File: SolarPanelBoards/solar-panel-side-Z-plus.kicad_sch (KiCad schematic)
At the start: 39 parts

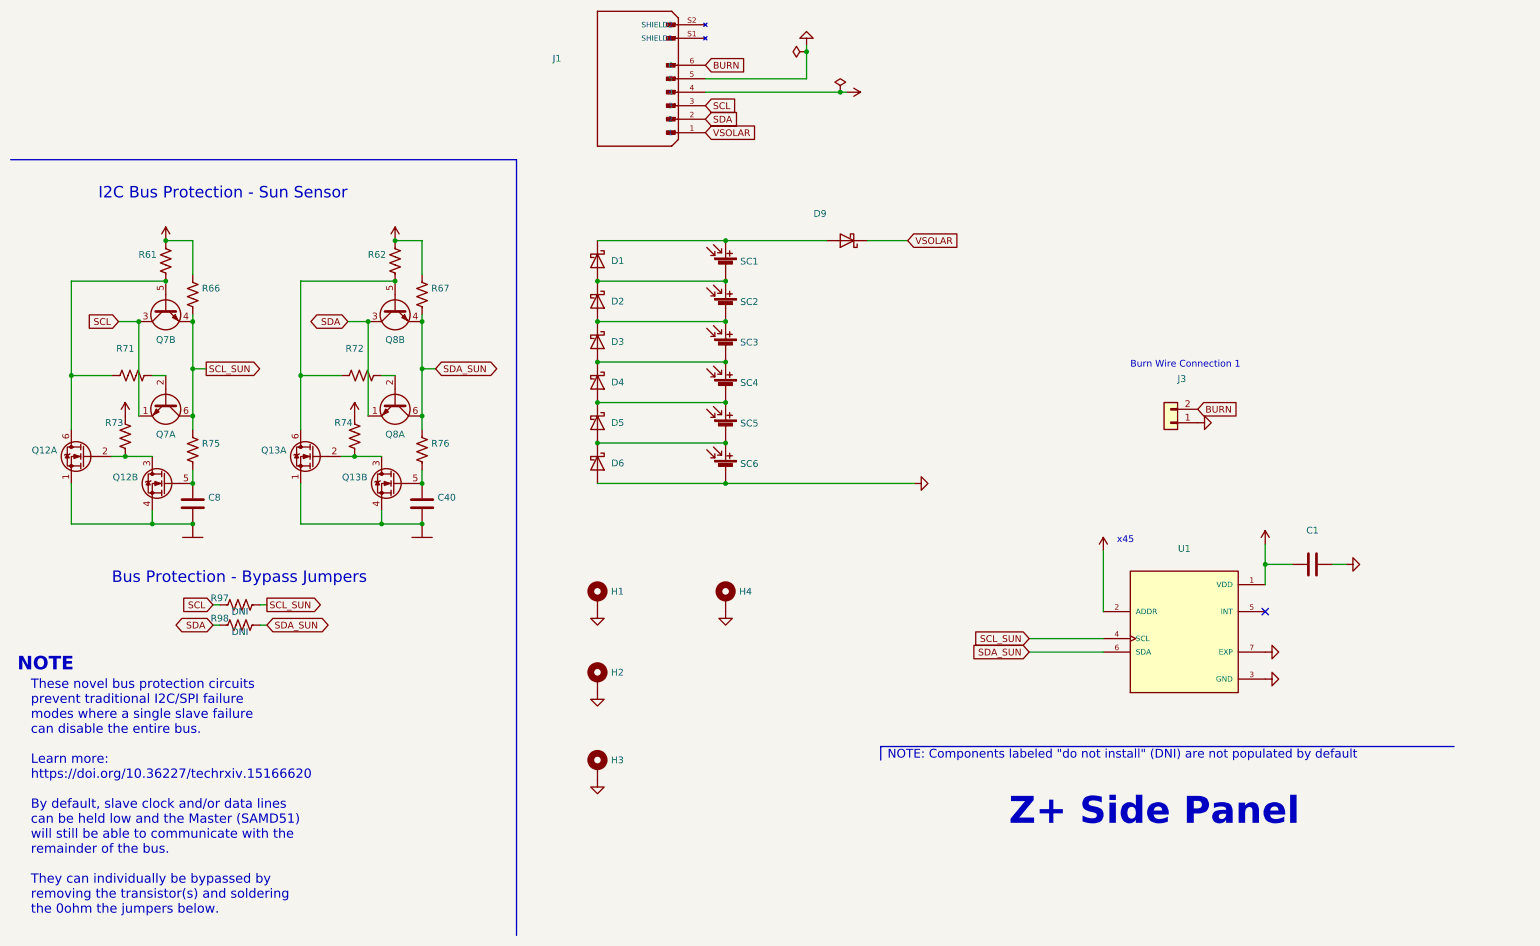
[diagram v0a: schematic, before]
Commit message: Final flight side panels w/ magnetorquers finished, note final board thickness of 0.031'' and updated copper weight of 0.5oz for internal layers
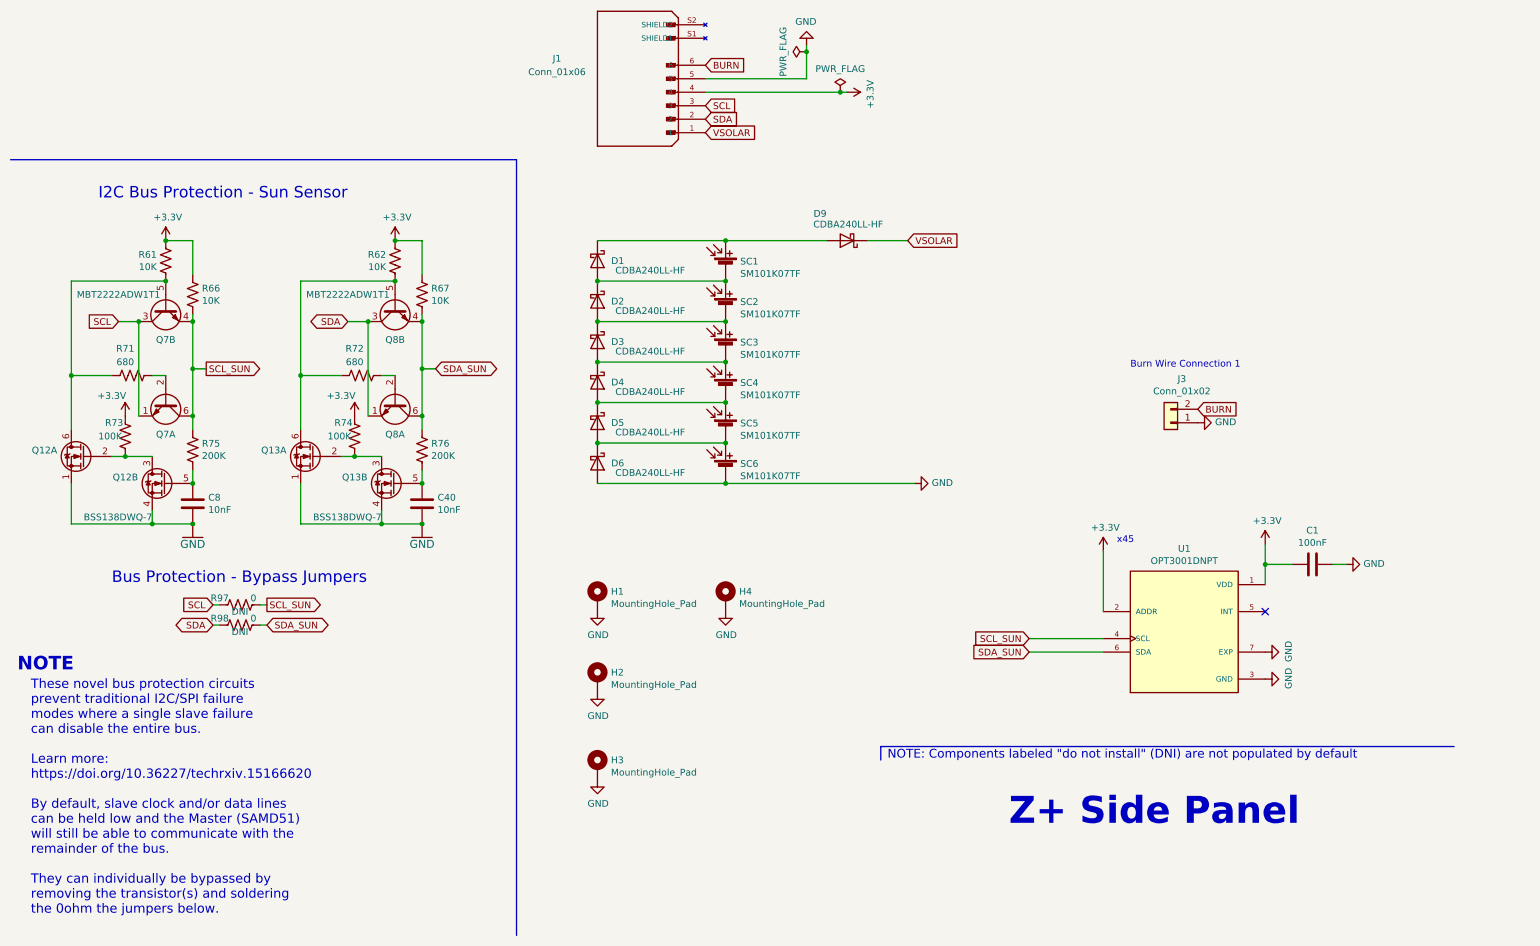
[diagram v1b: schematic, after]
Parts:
- C1: value (none) -> 100nF; footprint (none) -> Capacitor_SMD:C_0603_1608Metric
- C40, C8: value (none) -> 10nF; footprint (none) -> Capacitor_SMD:C_0603_1608Metric
- D1, D2, D3, D4, D5, D6, D9: value (none) -> CDBA240LL-HF; footprint (none) -> sapling:DO-214AC
- H1, H2, H3, H4: value (none) -> MountingHole_Pad; footprint (none) -> MountingHole:MountingHole_2.2mm_M2_DIN965_Pad_TopBottom
- J1: value (none) -> Conn_01x06; footprint (none) -> sapling:MOLEX_2053380006
- J3: value (none) -> Conn_01x02; footprint (none) -> sapling:Burn_Wire_Connection
- Q12, Q13: value (none) -> BSS138DWQ-7; footprint (none) -> sapling:BSS138DWQ-7
- Q7, Q8: value (none) -> MBT2222ADW1T1; footprint (none) -> Package_TO_SOT_SMD:SOT-363_SC-70-6
- R61, R62, R66, R67: value (none) -> 10K; footprint (none) -> Resistor_SMD:R_0603_1608Metric
- R71, R72: value (none) -> 680; footprint (none) -> Resistor_SMD:R_0603_1608Metric
- R73, R74: value (none) -> 100K; footprint (none) -> Resistor_SMD:R_0603_1608Metric
- R75, R76: value (none) -> 200K; footprint (none) -> Resistor_SMD:R_0603_1608Metric
- R97, R98: value (none) -> 0; footprint (none) -> Resistor_SMD:R_0603_1608Metric
- SC1, SC2, SC3, SC4, SC5, SC6: value (none) -> SM101K07TF; footprint (none) -> sapling:SM101K07TF
- U1: value (none) -> OPT3001DNPT; footprint (none) -> sapling:OPT3001
